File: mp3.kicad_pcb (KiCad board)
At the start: 2 copper layers, 58 x 79 mm, 45 parts, among them J1 AudioJack4_Ground, J2 AudioJack4_Ground, J3 Conn_01x08, J4 Micro_SD_Card_Det1, SW2 SW_Nidec_CAS-120A1, U1 XTAD5142IRGER, U2 MCP6002-xSN, U4 TP4056-42-ESOP8

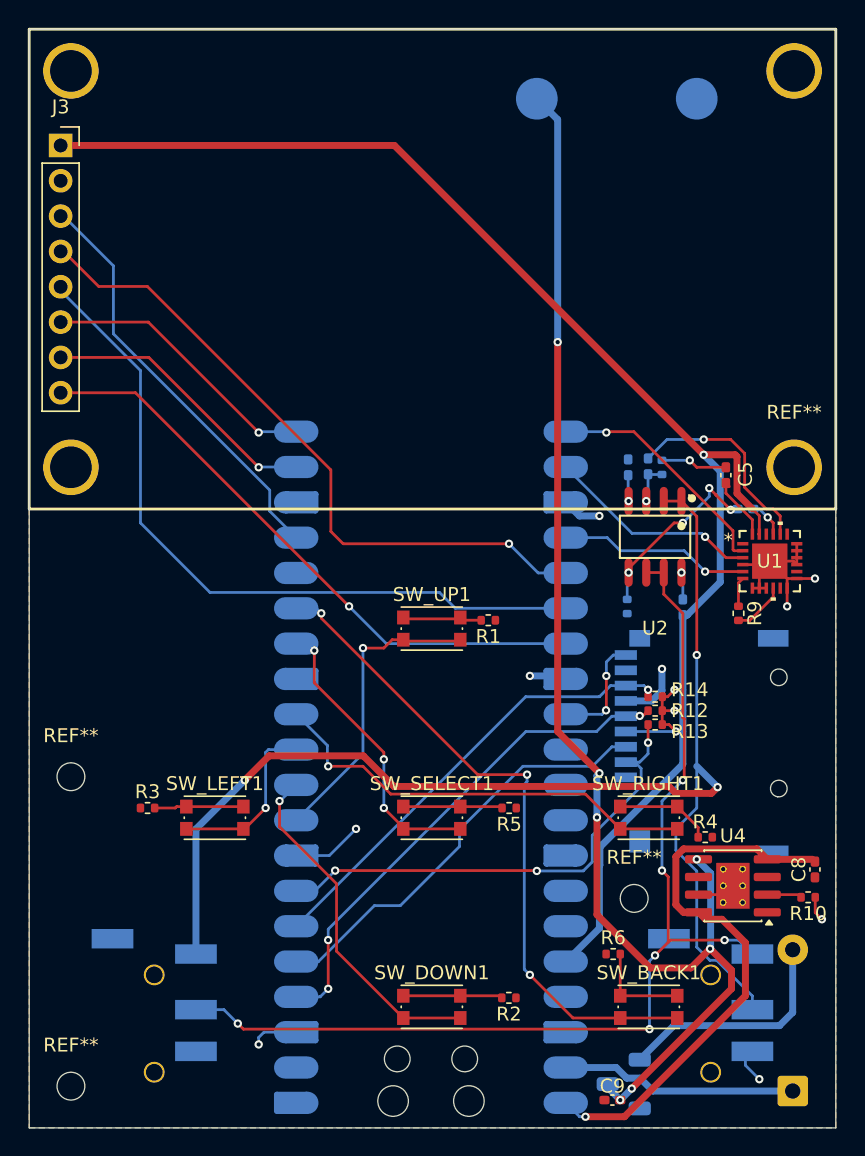
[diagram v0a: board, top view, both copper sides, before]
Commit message: Add voltage booster, optimizations
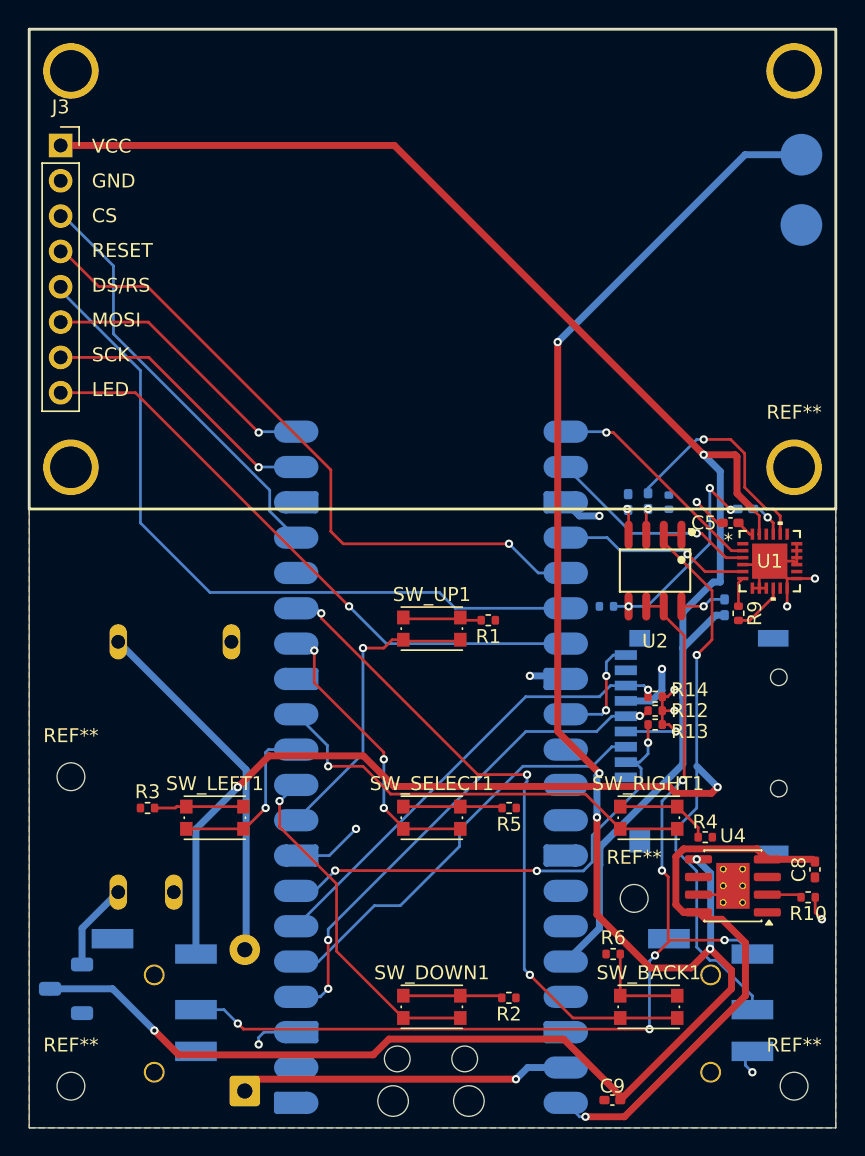
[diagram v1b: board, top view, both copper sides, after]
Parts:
- added CKCS_BS-2: ~, CKCS_BS-01:CKCS_BS-01, B.Cu at (29.0, 123.9)
- added REF**: MountingHole_2mm, MountingHole:MountingHole_2mm, F.Cu at (73.5, 147.0)
- moved SW2 40.7 mm to (21.1, 140.0)
- moved D1 39.4 mm to (34.0, 147.3)
- moved B+1 19.4 mm to (74.0, 80.0)
- moved B-1 11.8 mm to (74.0, 85.1)
- moved C5 3.45 mm to (68.9, 106.5), turned to 0 degrees
- moved C3 3.00 mm to (68.5, 112.6)
- moved R7 2.55 mm to (64.5, 105.0)
- moved C2 2.50 mm to (63.0, 104.9)
- moved C4 2.50 mm to (61.6, 105.0)
- moved U2 2.43 mm to (63.5, 109.9)
- moved R8 1.49 mm to (60.0, 112.5), turned to 180 degrees
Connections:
- SW2 pad 1: /Pico_VSYS -> /CKCS_IN
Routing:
- net +BATT: track 94.2 -> 143.2 mm, vias 7 -> 6
- net /Pico_VSYS: track 16.9 -> 26.0 mm
- net Net-(A1-VSYS): track 18.0 -> 24.7 mm, vias 0 -> 1
- net /CKCS_IN: track 0.00 -> 6.28 mm
- net /Pico_3V3: track 116.2 -> 120.8 mm
- net Net-(U2B--): track 77.3 -> 73.6 mm
- net Net-(U1-VREF): track 4.82 -> 1.33 mm
- net -BATT: track 48.7 -> 45.4 mm
- net Net-(U2B-+): track 13.6 -> 15.6 mm, vias 4 -> 3
- net Net-(U2A--): track 94.2 -> 92.6 mm
- net Net-(U2C-V+): track 1.97 -> 3.31 mm
- net Net-(U1-OUT1P): track 15.1 -> 16.3 mm
- net /Pico_I2S_SCK: track 17.1 -> 16.4 mm
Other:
- board text added: "CS"
- board text added: "DS/RS"
- board text added: "GND"
- board text added: "LED"
- board text added: "MOSI"
- board text added: "RESET"
- board text added: "SCK"
- board text added: "USB"
- board text added: "VCC"
- board text added: "microSD"

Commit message: Full re-routing
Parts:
- removed the REF** at (62.0, 133.5)
- removed the REF** at (73.5, 102.5)
- removed the REF** at (21.5, 124.8)
- added ?: , , F.Cu at (126.2, 82.8)
- C1, C2, C3, C4, J4, R7, R8: moved to F.Cu
- R10: moved to B.Cu
- moved SW2 126.8 mm to (126.3, 69.2)
- moved D1 110.1 mm to (126.0, 86.8), turned to -90 degrees
- moved J2 94.6 mm to (120.0, 120.8)
- moved C9 88.1 mm to (122.1, 85.0), turned to 0 degrees
- moved J4 77.1 mm to (121.7, 68.5), turned to 90 degrees
- moved U4 71.9 mm to (119.6, 81.4), turned to 0 degrees
- moved CKCS_BS-2 71.5 mm to (100.4, 121.1), turned to 180 degrees
- moved R13 66.7 mm to (106.5, 70.0), turned to 0 degrees
- moved R12 65.2 mm to (106.5, 71.0), turned to 0 degrees
- moved R14 63.7 mm to (106.5, 72.0), turned to 0 degrees
- moved C8 62.6 mm to (116.9, 85.0), turned to 180 degrees
- moved R10 58.2 mm to (106.0, 84.5), turned to 90 degrees
- moved SW_BACK1 56.3 mm to (115.8, 121.6)
- moved R1 56.3 mm to (104.2, 93.8)
- moved R5 56.3 mm to (105.8, 107.3)
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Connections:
- J1 pad 3: Net-(U2A--) -> Net-(U2B--)
- J1 pad 4: Net-(U2B--) -> Net-(U2A--)
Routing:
- net -BATT: track 45.4 -> 172.2 mm, vias 10 -> 34
- net +BATT: track 143.2 -> 32.0 mm, vias 6 -> 2
- net /CKCS_IN: track 6.28 -> 72.0 mm, vias 0 -> 1
- net /Pico_I2S_SCK: track 16.4 -> 67.4 mm
- net /Pico_I2S_FSYNC: track 15.4 -> 63.5 mm
- net Net-(A1-VSYS): track 24.7 -> 71.4 mm, vias 1 -> 0
- net Net-(U2B--): track 73.6 -> 116.8 mm, vias 6 -> 3
- net /Pico_I2S_SD: track 13.8 -> 55.7 mm
- net /SCREEN_SDI_MOSI: track 20.9 -> 61.6 mm
- net /SD_DET: track 8.11 -> 46.8 mm, vias 2 -> 1
- net /SCREEN_SCK: track 20.2 -> 57.1 mm
- net /Pico_VBUS: track 41.4 -> 77.0 mm, vias 1 -> 3
- net /Pico_VSYS: track 26.0 -> 58.4 mm, vias 0 -> 1
- net /SD_CLK: track 36.3 -> 68.1 mm
- net /BTN_LEFT: track 12.5 -> 43.6 mm
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
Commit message: Fix diode direction
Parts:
- moved D1 10.2 mm to (126.0, 97.1), turned to 90 degrees
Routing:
- net /Pico_VSYS: track 58.4 -> 69.8 mm
- net -BATT: track 172.2 -> 165.3 mm
- net Net-(A1-VSYS): track 71.4 -> 67.6 mm, vias 0 -> 4

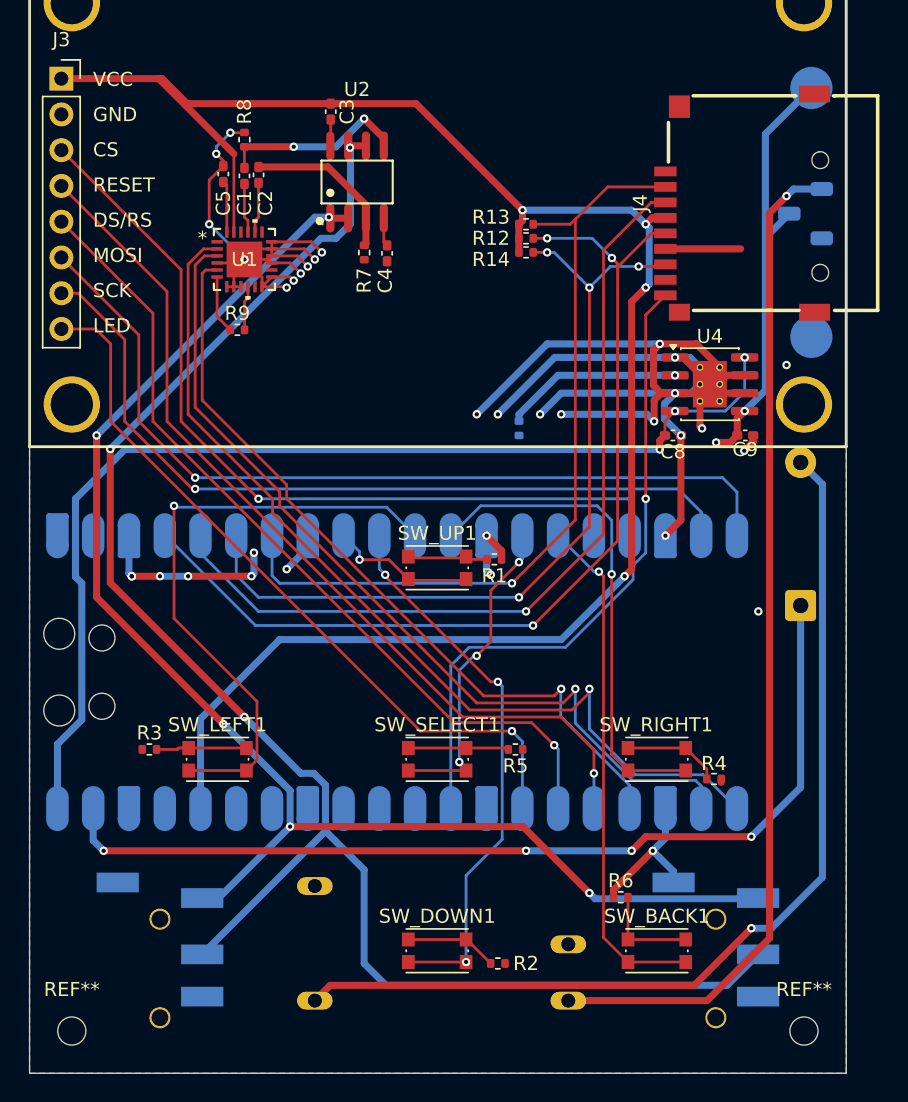
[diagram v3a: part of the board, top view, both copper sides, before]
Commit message: Add new battery management system
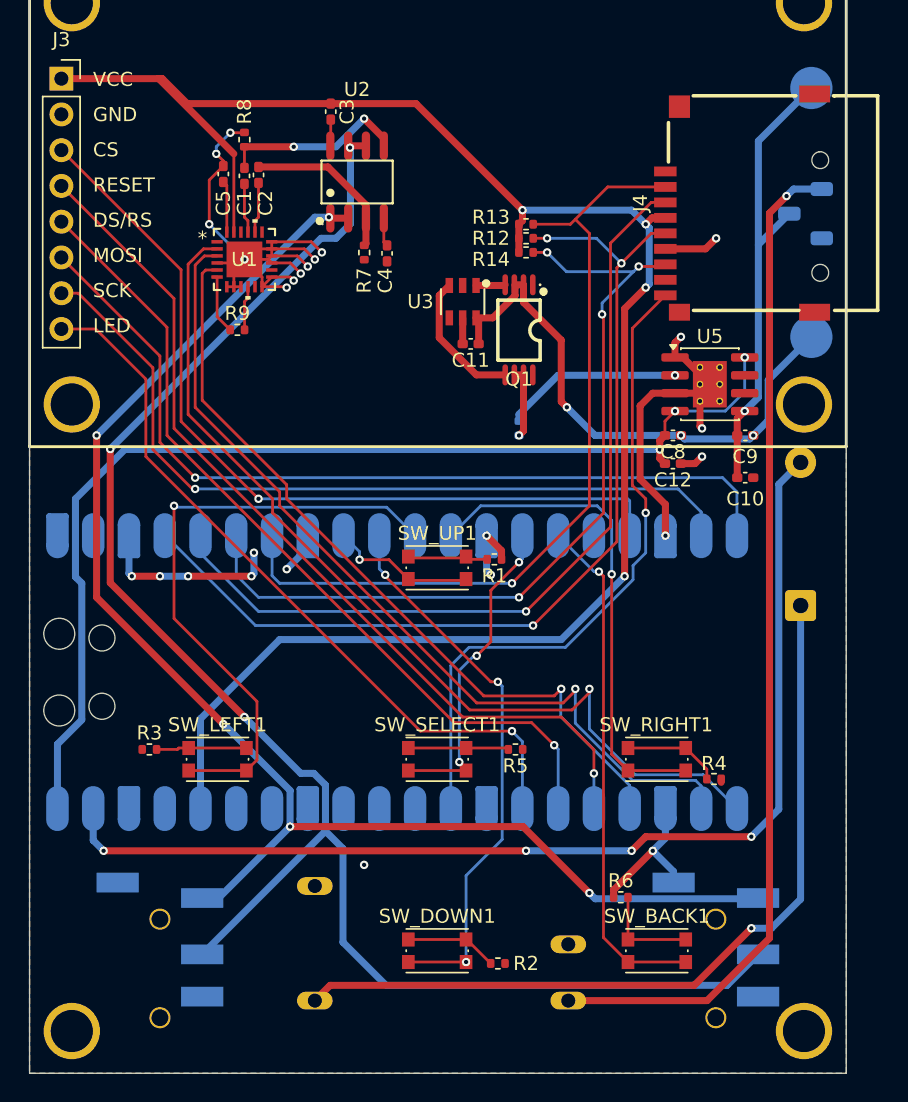
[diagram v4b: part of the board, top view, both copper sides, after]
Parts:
- removed REF** (x2): MountingHole_2mm, MountingHole:MountingHole_2mm
- added ?: , , F.Cu at (74.2, 127.3)
- added ?: , , F.Cu at (126.2, 127.3)
- added C10: 10uF, Capacitor_SMD:C_0402_1005Metric_Pad0.74x0.62mm_HandSolder, F.Cu at (122.1, 88.0)
- added C11: 0.1uF, Capacitor_SMD:C_0402_1005Metric_Pad0.74x0.62mm_HandSolder, F.Cu at (102.6, 78.5)
- added C12: 0.1uF, Capacitor_SMD:C_0402_1005Metric_Pad0.74x0.62mm_HandSolder, F.Cu at (116.9, 87.0)
- added Q1: 8205A_C14212, JLCPCB_Misc:TSSOP-8_L4.4-W3.0-P0.65-LS6.4-BL-2, F.Cu at (106.0, 77.5)
- added U3: DW01A_C351410, JLCPCB_Power_Management_ICs:SOT-23-6_L2.9-W1.6-P0.95-LS2.8-BL, F.Cu at (102.0, 75.5)
- turned R10 to -90 degrees
- renumbered U4 to U5
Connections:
- A1 pad 13: -BATT -> GND
- A1 pad 18: -BATT -> GND
- A1 pad 23: -BATT -> GND
- A1 pad 28: -BATT -> GND
- A1 pad 3: -BATT -> GND
- A1 pad 38: -BATT -> GND
- A1 pad 8: -BATT -> GND
- C4 pad 2: -BATT -> GND
- C5 pad 1: -BATT -> GND
- CKCS_BS-2 pad 2: -BATT -> GND
- CKCS_BS-2 pad 4: -BATT -> GND
- D1 pad 1: Net-(A1-VSYS) -> /Pico_VSYS
- D1 pad 2: /Pico_VSYS -> Net-(A1-VSYS)
- J1 pad 1: -BATT -> GND
- J1 pad 2: -BATT -> GND
- J2 pad 1: -BATT -> GND
- J2 pad 2: -BATT -> GND
- J3 pad 2: -BATT -> GND
- J4 pad 6: -BATT -> GND
- R1 pad 1: -BATT -> GND
- R10 pad 1: -BATT -> Net-(U5-PROG)
- R10 pad 2: Net-(U4-PROG) -> GND
- R2 pad 1: -BATT -> GND
- R3 pad 1: -BATT -> GND
- R4 pad 1: -BATT -> GND
- R5 pad 1: -BATT -> GND
- R6 pad 1: -BATT -> GND
- R7 pad 1: -BATT -> GND
- R8 pad 2: -BATT -> GND
- U1 pad 12: -BATT -> GND
- U1 pad 13: -BATT -> GND
- U1 pad 15: -BATT -> GND
- U1 pad 16: -BATT -> GND
- U1 pad 17: -BATT -> GND
- U1 pad 18: -BATT -> GND
- U1 pad 25: -BATT -> GND
- U1 pad 4: -BATT -> GND
- U1 pad 7: -BATT -> GND
- U1 pad 8: -BATT -> GND
- U1 pad 9: -BATT -> GND
- U5 pad 1: -BATT -> GND
- U5 pad 2: Net-(U4-PROG) -> Net-(U5-PROG)
- U5 pad 3: -BATT -> GND
- U5 pad 6: -BATT -> Net-(U5-~{STDBY})
- U5 pad 7: -BATT -> Net-(U5-~{CHRG})
- U5 pad 9: -BATT -> GND
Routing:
- net -BATT: track 165.3 -> 39.7 mm, vias 34 -> 3
- net GND: track 0.00 -> 107.6 mm, vias 0 -> 26
- net Net-(U5-PROG): track 0.00 -> 12.7 mm, vias 0 -> 1
- net Net-(U4-PROG): track 12.7 -> 0.00 mm, vias 1 -> 0
- net /Pico_VSYS: track 69.8 -> 58.3 mm
- net Net-(A1-VSYS): track 67.6 -> 77.8 mm
- net Net-(Q1-G2): track 0.00 -> 9.79 mm
- net Net-(Q1-G1): track 0.00 -> 2.09 mm
- net Net-(U3-VCC): track 0.00 -> 1.85 mm
- net /SD_MISO: track 58.7 -> 60.3 mm
- net /Pico_VBUS: track 77.0 -> 78.1 mm
- net +BATT: track 32.0 -> 33.0 mm, vias 2 -> 1
- net /SD_CS: track 59.0 -> 59.9 mm
- net /SD_DET: track 46.8 -> 47.6 mm
- added copper zone on B.Cu, net GND
- added copper zone on F.Cu, net GND
- removed copper zone on B.Cu, net -BATT
- removed copper zone on F.Cu, net -BATT

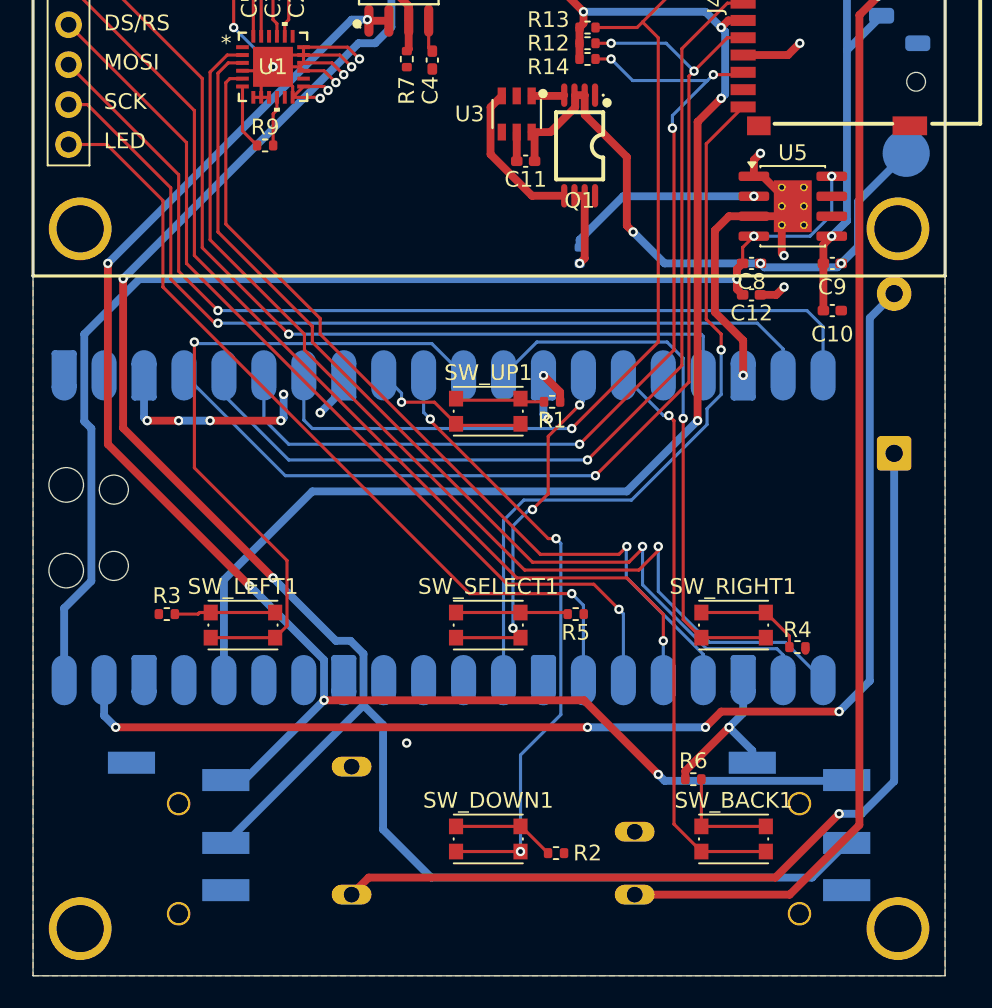
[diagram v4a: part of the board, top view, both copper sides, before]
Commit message: Move Pico and audio jacks closer to PCB border
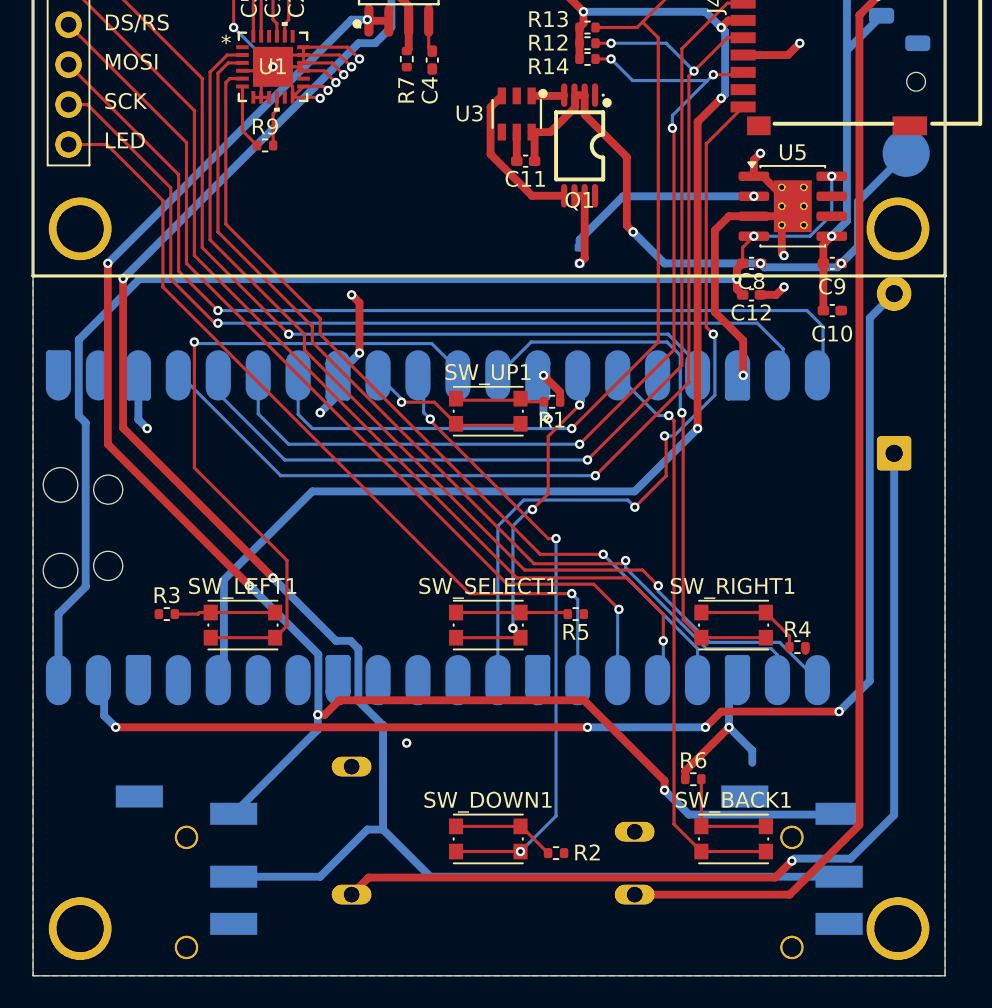
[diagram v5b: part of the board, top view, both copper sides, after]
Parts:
- added REF**: 703048 3.7V 1200mAh Battery, 703048:703048 3.7V 1200mAh Battery, B.Cu at (100.2, 68.5)
- moved J1 2.20 mm to (81.0, 123.0)
- moved J2 2.20 mm to (119.5, 123.0)
- moved A1 0.36 mm to (97.0, 101.8)
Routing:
- net GND: track 107.6 -> 103.8 mm, vias 26 -> 24
- net /Pico_I2S_SCK: track 67.4 -> 64.2 mm
- net Net-(U2B--): track 116.8 -> 113.8 mm
- net Net-(U2A--): track 101.5 -> 104.0 mm
- net /Pico_I2S_FSYNC: track 63.5 -> 61.3 mm
- net /Pico_I2S_SD: track 55.7 -> 53.9 mm
- net /SCREEN_CS: track 59.5 -> 58.1 mm
- net /Pico_VSYS: track 58.3 -> 59.6 mm
- net /SD_DET: track 47.6 -> 48.6 mm, vias 1 -> 3
- net /BTN_BACK: track 36.6 -> 37.4 mm
